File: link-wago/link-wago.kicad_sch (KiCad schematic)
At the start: 29 parts, among them J101 2x05_Horizontal, J102 NE8FAH, J103 JAE_DX07S016JA3, J104 2x05_Horizontal, J105 NE8FAH, J106 Conn_01x01, J107 Conn_01x01, J108 WAGO-2065, J109 WAGO-2065, J110 WAGO-2065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

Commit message: Refresh
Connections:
- net +24V-Supply renamed +24V-Link

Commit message: Update
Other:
- note added: "PoE Passive +24V IEEE 802.3af Mode B"
- note added: "RS-422 3MHz"
- note added: "The cables used to connect the device and the power adapter reverse the order of the wires."
- note added: "V2 Link – WAGO"
- note removed: "The cables connecting the device and the power adapter reverse the order of the wires. So these connectors are different from the otherwise identical connectors at the device."
- note removed: "V2 Link"
- moved on the sheet: C101, J106, J107, J108, J109, J110, J111, TVS101

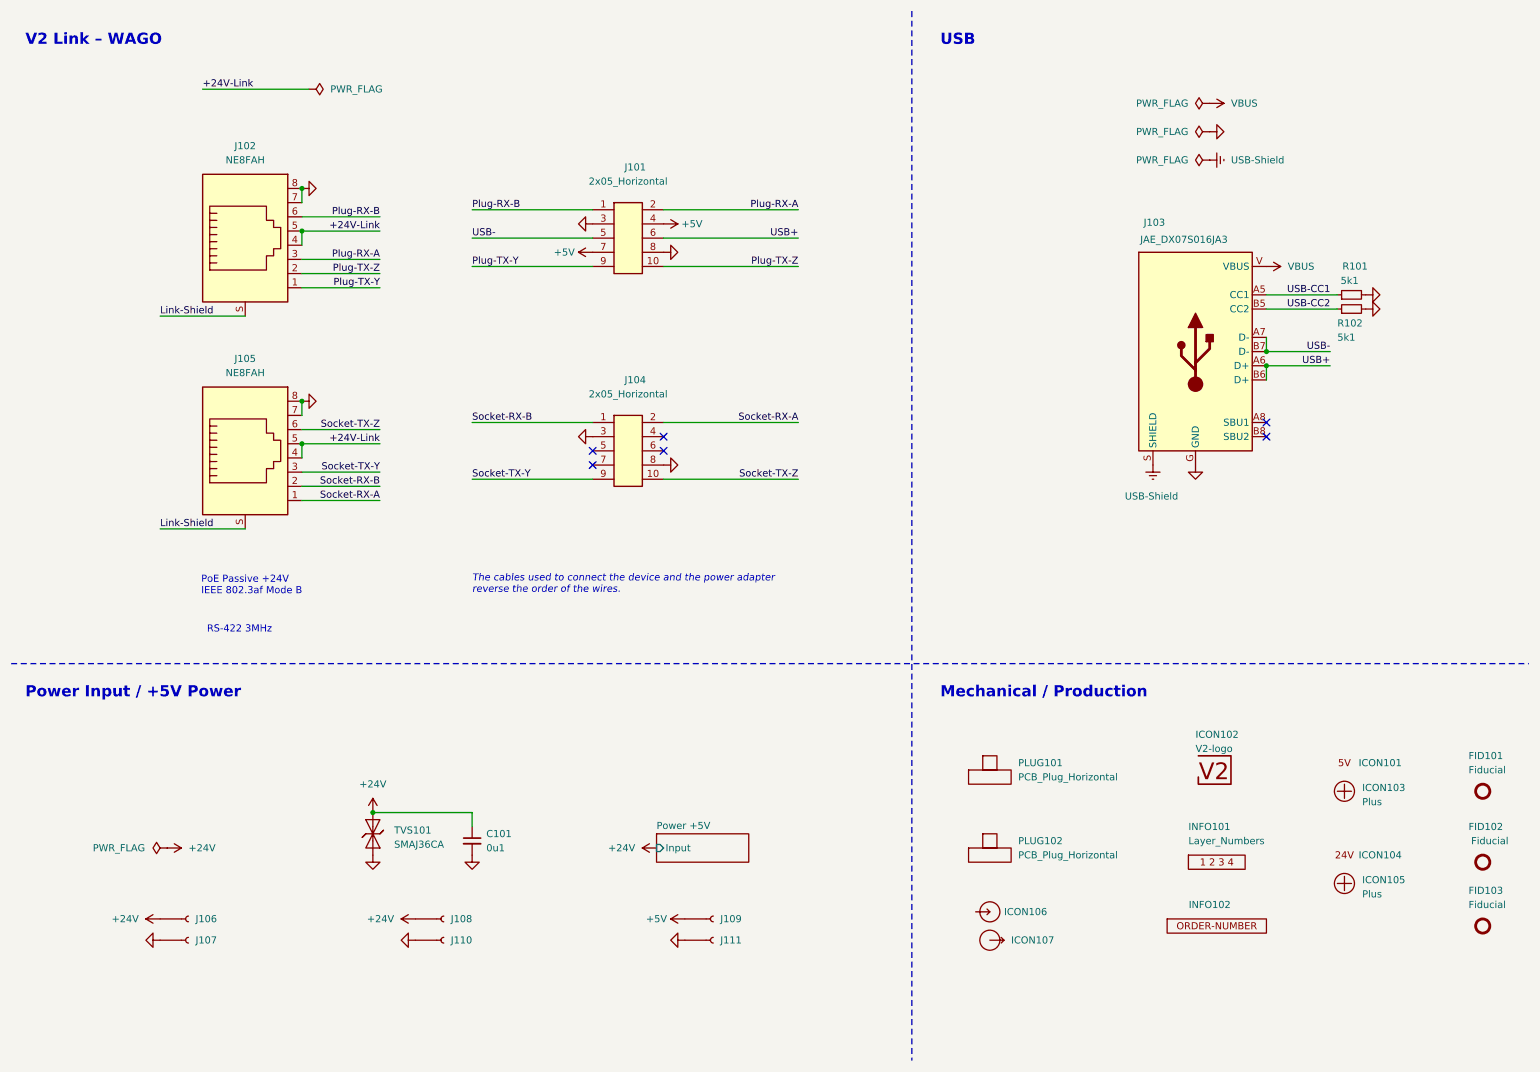
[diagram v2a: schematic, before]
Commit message: Update power symbols
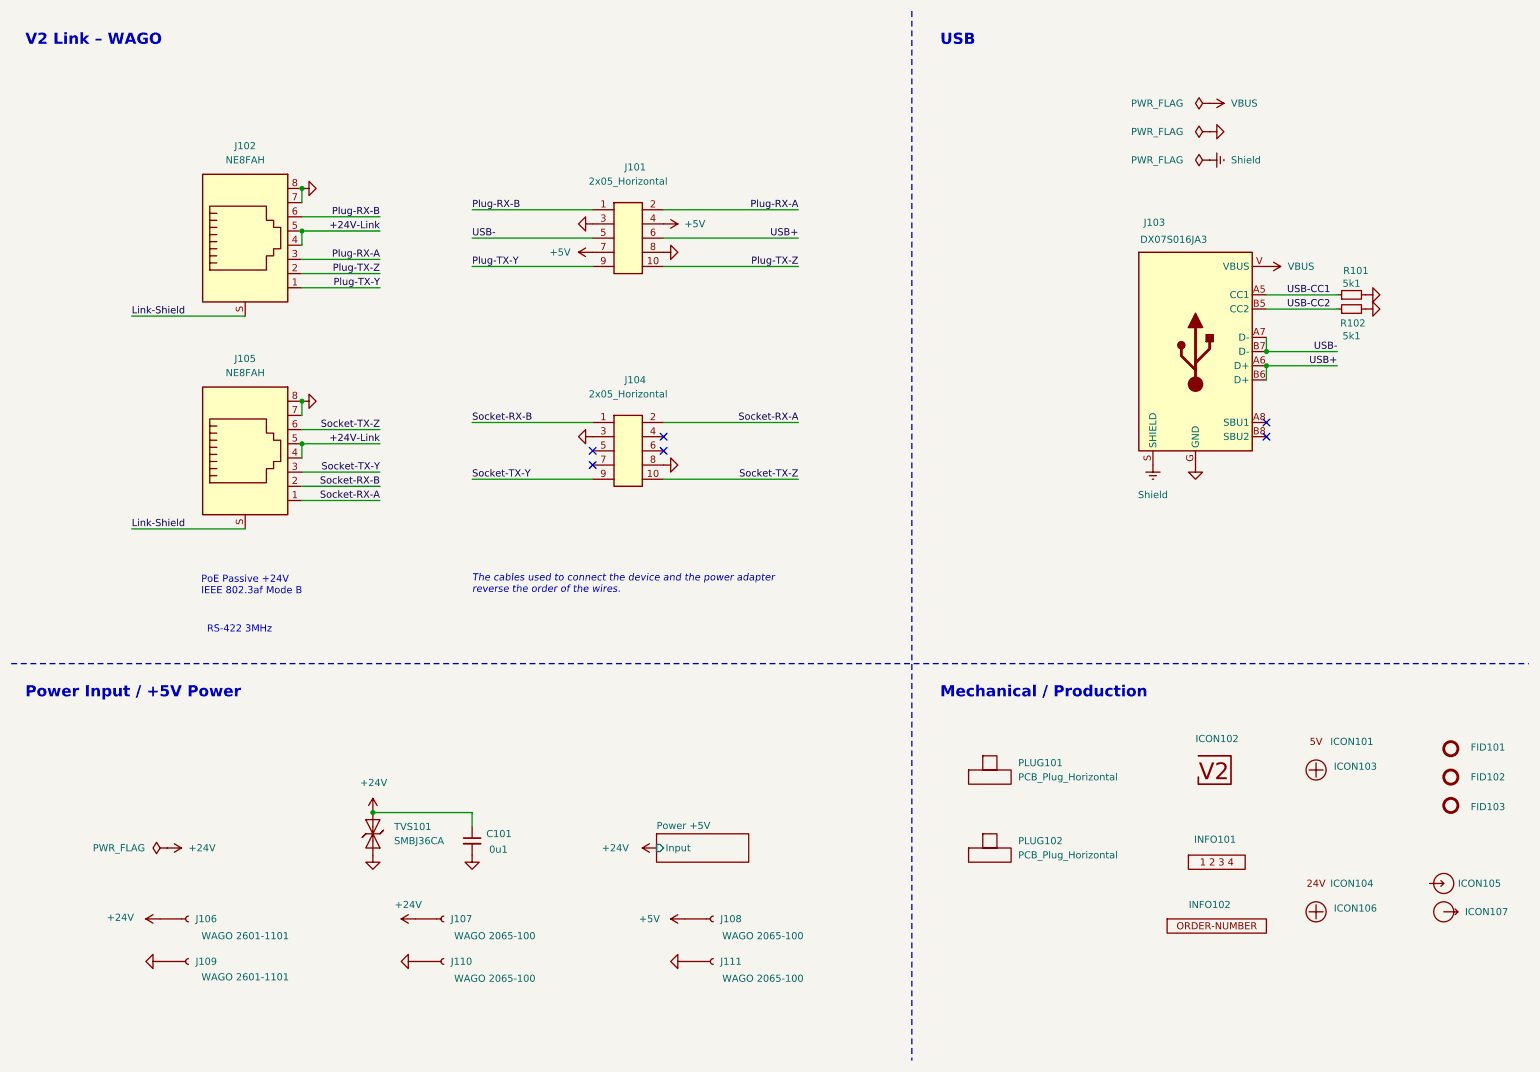
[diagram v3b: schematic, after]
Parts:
- C101: footprint Capacitor_SMD:C_0603_1608Metric -> V2_Capacitor_SMD:C_0603; symbol Device:C_Small -> V2_Device:C_0603_0u1; Mouser (none) -> 810-CGA3E2X7R1H104MA
- FID101, FID102, FID103: value Fiducial -> Fiducial_Paste
- ICON102: footprint V2_Artwork:Logo_Tiny -> V2_Artwork:Logo_Small
- INFO102: value ORDER-NUMBER -> Order_Number
- J101, J104: Mouser (none) -> 649-200211120001T4LF
- J102, J105: Mouser (none) -> 568-NE8FAH
- J103: value JAE_DX07S016JA3 -> DX07S016JA3; Mouser (none) -> 656-DX07S016JA3R1500
- J106: value Conn_01x01 -> WAGO 2601-1101
- J107: renamed from J108; value WAGO-2065 -> WAGO 2065-100
- J108: renamed from J109; value WAGO-2065 -> WAGO 2065-100
- J109: renamed from J107; value Conn_01x01 -> WAGO 2601-1101
- J110, J111: value WAGO-2065 -> WAGO 2065-100
- R101, R102: footprint Resistor_SMD:R_0603_1608Metric -> V2_Resistor_SMD:R_0603; symbol Device:R_Small -> V2_Device:R_0603_5k1; Mouser (none) -> 71-CRCW06035K10FKEAC
- TVS101: value SMAJ36CA -> SMBJ36CA; footprint Diode_SMD:D_SMA -> V2_Diode_SMD:D_SMB; symbol V2_Diode:SMAJ36CA -> V2_Diode:SMBJ36CA; Mouser (none) -> 652-SMBJ36CA-Q
- renumbered ICON106 to ICON105, ICON105 to ICON106
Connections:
- net USB-Shield renamed Shield
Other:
- moved on the sheet: FID101, FID102, FID103, ICON101, ICON103, ICON104, ICON105, ICON106, ICON107, J109, J110, J111

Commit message: Refresh
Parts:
- C101: Manufacturer (none) -> TDK; Product (none) -> CGA3E2X7R1H104M080AA
- J101, J104: Manufacturer (none) -> Amphenol FCI; Product (none) -> 20021112-00010T4LF
- J102, J105: Manufacturer (none) -> Neutrik; Product (none) -> NE8FAH
- J103: Manufacturer (none) -> JAE Electronics; Product (none) -> DX07S016JA3R1500
- J106, J109: Manufacturer (none) -> WAGO; Product (none) -> 2601-1101
- J107, J108, J110, J111: Manufacturer (none) -> WAGO; Product (none) -> 2065-100/998-403
- R101, R102: Manufacturer (none) -> Vishay; Product (none) -> CRCW06035K10FKEAC; Rating (none) -> 100mW
- TVS101: Manufacturer (none) -> Bourns; Product (none) -> SMBJ36CA-Q; Rating (none) -> 36V

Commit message: Fix WAGOs
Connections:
- net +24V-Link renamed +VLINK
- net VBUS renamed +VBUS

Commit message: Refresh
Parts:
- C101: Rating (none) -> 50V

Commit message: Refresh
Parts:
- ICON104: value 24V -> (none); footprint V2_Artwork:24V -> V2_Artwork:28V; symbol V2_Artwork:24V -> V2_Artwork:28V
- TVS101: value SMBJ36CA -> SMBJ33CA; symbol V2_Diode:SMBJ36CA -> V2_Diode:SMBJ33CA; Mouser 652-SMBJ36CA-Q -> 652-SMBJ33CA-Q; Product SMBJ36CA-Q -> SMBJ33CA-Q; Rating 36V -> 33V
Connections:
- net +24V renamed +28V
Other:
- moved on the sheet: C101, J106, J107, J108, J109, J110, J111, TVS101

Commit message: Update library
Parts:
- ICON104: value (none) -> ~
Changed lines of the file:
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@@
 			)
 		)
-		(property "Value" ""
+		(property "Value" "~"
 			(at 246.38 173.99 0)
 			(effects
